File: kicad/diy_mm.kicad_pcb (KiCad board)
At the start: 2 copper layers, 59.5 x 8 mm, 31 parts, among them Q1 BC859C, Q2 BC859C, Q3 BC859C, Q4 BC849C

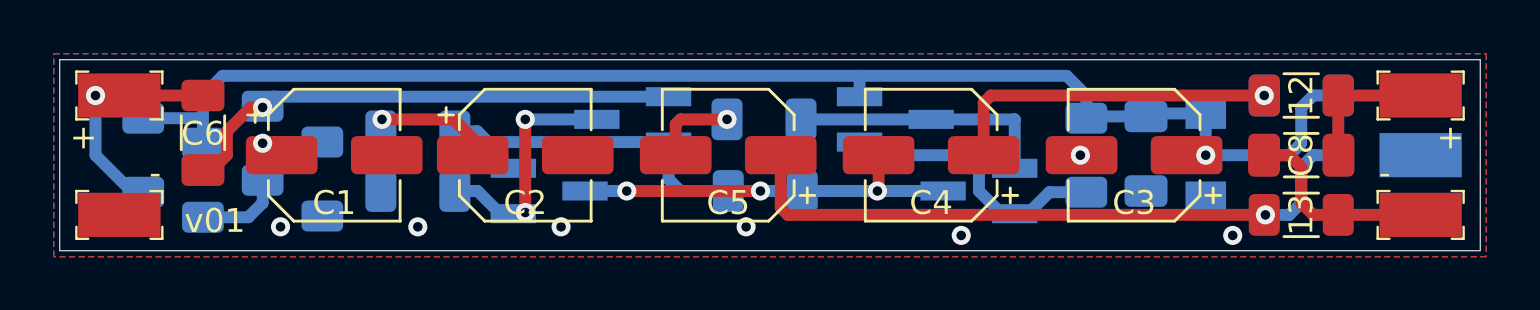
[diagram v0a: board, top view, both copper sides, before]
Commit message: redesign for KiCad 6.0.1
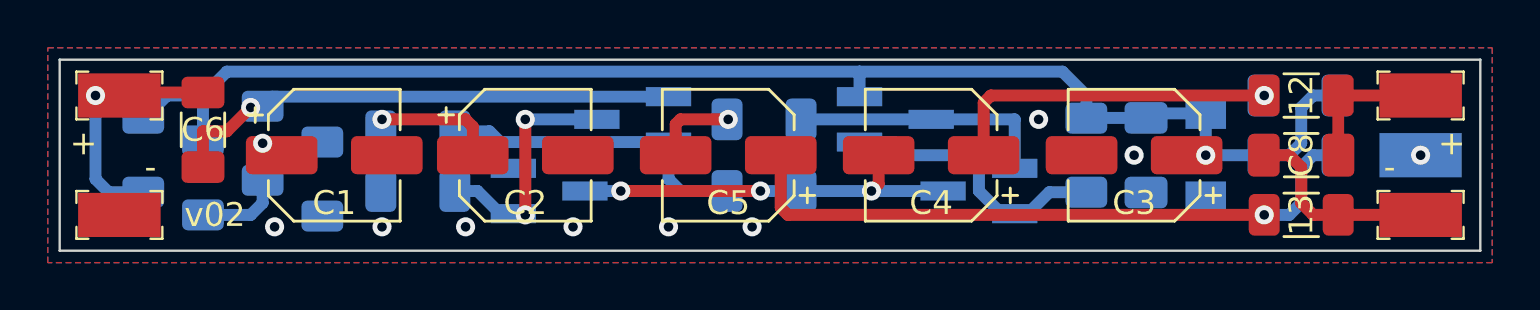
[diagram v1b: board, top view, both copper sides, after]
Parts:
- removed +: mic+, digikey-footprints:PC_TEST_POINT_SMD
- removed +: XLR2, digikey-footprints:PC_TEST_POINT_SMD
- removed -: mic-, digikey-footprints:PC_TEST_POINT_SMD
- removed -: XLR3, digikey-footprints:PC_TEST_POINT_SMD
- removed 10, 11: 2.2k, Resistor_SMD:R_1206_3216Metric_Pad1.30x1.75mm_HandSolder
- removed 12, 13: 100, Resistor_SMD:R_1206_3216Metric_Pad1.30x1.75mm_HandSolder
- removed GND: XLR1, digikey-footprints:PC_TEST_POINT_SMD
- added J1: mic+, digikey-footprints:PC_TEST_POINT_SMD, F.Cu at (102.5, 101.5)
- added J2: mic-, digikey-footprints:PC_TEST_POINT_SMD, F.Cu at (102.5, 106.5)
- added J3: XLR2, digikey-footprints:PC_TEST_POINT_SMD, F.Cu at (157.0, 101.5)
- added J4: XLR1, digikey-footprints:PC_TEST_POINT_SMD, B.Cu at (157.0, 104.0)
- added J5: XLR3, digikey-footprints:PC_TEST_POINT_SMD, F.Cu at (157.0, 106.5)
- added R10: 2.2k, Resistor_SMD:R_1206_3216Metric_Pad1.30x1.75mm_HandSolder, B.Cu at (151.9, 101.5)
- added R11: 2.2k, Resistor_SMD:R_1206_3216Metric_Pad1.30x1.75mm_HandSolder, B.Cu at (151.9, 104.0)
- added R12: 100, Resistor_SMD:R_1206_3216Metric_Pad1.30x1.75mm_HandSolder, F.Cu at (152.0, 101.5)
- added R13: 100, Resistor_SMD:R_1206_3216Metric_Pad1.30x1.75mm_HandSolder, F.Cu at (152.0, 106.5)
- moved C6 0.12 mm to (106.0, 102.9), turned to -90 degrees
- moved R1 0.10 mm to (106.0, 105.0)
- moved C7 0.06 mm to (145.5, 104.0), turned to -90 degrees
- moved R4 0.05 mm to (129.5, 105.5), turned to 0 degrees
- turned C8 to 180 degrees
- turned R9 to 90 degrees
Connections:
- C1 pad 2: Earth -> GND
- C2 pad 2: Earth -> GND
- C3 pad 2: Earth -> GND
- C5 pad 2: Earth -> GND
- C7 pad 1: Earth -> +10V
- C7 pad 2: +10V -> GND
- D1 pad 2: Earth -> GND
- Q1 pad 1: Net-(C6-Pad1) -> Net-(C6-Pad2)
- Q4 pad 2: Earth -> GND
- R2 pad 1: Net-(C6-Pad1) -> Net-(C6-Pad2)
- R3 pad 2: Earth -> GND
- R4 pad 1: Net-(C4-Pad2) -> Net-(Q1-Pad2)
- R4 pad 2: Net-(Q1-Pad2) -> Net-(C4-Pad2)
- R5 pad 2: Earth -> GND
- R6 pad 2: Earth -> GND
- R7 pad 2: Net-(C6-Pad2) -> Net-(C6-Pad1)
- R9 pad 1: +10V -> Net-(Q2-Pad1)
- R9 pad 2: Net-(Q2-Pad1) -> +10V
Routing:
- net Net-(C6-Pad2): track 8.64 -> 21.1 mm
- net Net-(C6-Pad1): track 21.3 -> 9.28 mm
- net GND: track 0.00 -> 3.63 mm, vias 0 -> 10
- net Earth: track 3.53 -> 0.00 mm, vias 8 -> 0
- net Net-(C8-Pad1): track 8.58 -> 6.03 mm
- net Net-(C10-Pad1): track 6.06 -> 8.48 mm
- added copper zone on B.Cu, net GND
- added copper zone on F.Cu, net GND
- removed copper zone on B.Cu, net Earth
- removed copper zone on F.Cu, net Earth
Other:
- net class Default removed
- board text added: "(c)hf"
- board text added: "v02"
- board text removed: "(c)FH"
- board text removed: "v01"
